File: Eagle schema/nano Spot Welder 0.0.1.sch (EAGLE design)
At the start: 32 parts, among them Q2 BC548, T1 BTA 41 / 600V, U1 NANO, U2 DISPLAY-NOKIA-5110, U3 DS18B20, X3 ~230V, X4 Mikro trafó

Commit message: - átszervezés
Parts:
- added Q1: BC548, transistor-npn:BC548
- added Q3: BC138, transistor-npn:BC548
- added R10, R9: 10k, resistor:R-EU_0204/7
- added VT1: Ventilátor, con-ptr500:AK300/2
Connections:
- net N$10 renamed A2
- net N$12 renamed A0
- net N$13 renamed D10
- net N$14 renamed +3.3V
- net N$2 renamed D9
- net N$27 renamed A1
- net N$3 renamed D8
- net N$30 renamed D11
- net N$4 renamed D7
- net N$5 renamed D6
- net N$6 renamed D5
- net N$7 renamed D4
- net N$8 renamed D3
- net N$9 renamed D2
- removed net N$11: R3.1, U1.D13
- removed net N$17: BUZZER1.2, Q2.C
- new net A3: R10.1, U1.A3
- new net D12: R9.2, U1.D12, U1.D13
- new net D13: R3.1
- new net N$3: BUZZER1.1, Q2.C
- new net N$4: Q1.B, R9.1
- new net N$5: Q3.B, R10.2
- new net N$6: Q3.C, VT1-1.KL
- net GND: now also Q3.E; no longer U1.GND2
- net MOC: now also Q1.E; no longer U1.D12
- net N$28: now also R5.1
- net N$33: no longer R5.1
- net VCC: now also BUZZER1.2, Q1.C, VT1-2.KL; no longer BUZZER1.1
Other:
- moved on the sheet: B1, BUZZER1, C10, C9, F1, KY-040, LED1, LED2, OK1, OK2, Q2, R1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

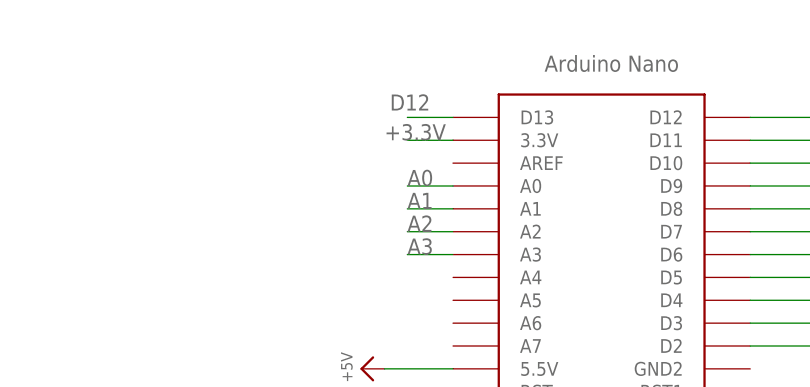
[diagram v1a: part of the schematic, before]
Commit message: - kijelzés finomítás - DS18B20 kiiktatása a próbák alatt
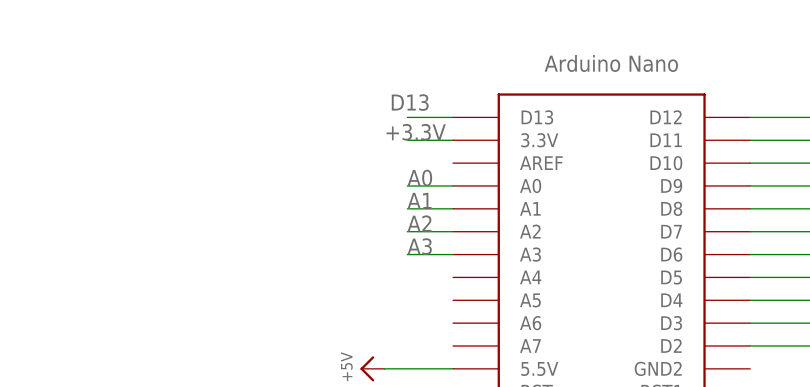
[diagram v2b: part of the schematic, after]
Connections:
- net D12: no longer U1.D13
- net D13: now also U1.D13
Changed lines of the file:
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@@
 <label x="-17.78" y="33.02" size="1.778" layer="95"/>
+</segment>
+<segment>
+<pinref part="U1" gate="G$1" pin="D13"/>
+<wire x1="-48.26" y1="119.38" x2="-53.34" y2="119.38" width="0.1524" layer="91"/>
+<label x="-50.8" y="121.92" size="1.778" layer="95" rot="R180"/>
 </segment>
 </net>
@@
 <label x="-101.6" y="-22.86" size="1.778" layer="95"/>
 </segment>
-<segment>
-<pinref part="U1" gate="G$1" pin="D13"/>
-<wire x1="-48.26" y1="119.38" x2="-53.34" y2="119.38" width="0.1524" layer="91"/>
-<label x="-50.8" y="121.92" size="1.778" layer="95" rot="R180"/>
-</segment>
 </net>

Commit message: - Eagle schema update
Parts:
- added D1: 1N4148, diode:1N4148DO35-10
- added J1: (no value), SparkFun-Connectors:CONN_03X22X3_SILK_MALE_PTH
- added R11: 1k, resistor:R-EU_0204/7
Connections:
- new net RST: J1.5, R11.1, U1.RST
- net D11: now also J1.4
- net D12: now also J1.1
- net D13: now also J1.3
- net GND: now also D1.A, J1.6, U1.GND2
- net N$6: now also D1.C
- net VCC: now also J1.2, R11.2, U1.AREF
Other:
- note added: "ISP"
- note added: "KY-040 Rotary Encoder"
- note added: "MOT Temperature Measurement"
- moved on the sheet: LED2, R1, R7, R8, S1, U2

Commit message: - próbapanel javítgatások
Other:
- note added: "CLK"
- note added: "DT"
- note added: "SW"
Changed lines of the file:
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@@
 <text x="116.84" y="45.72" size="1.778" layer="91">KY-040 Rotary Encoder</text>
 <text x="109.22" y="-20.32" size="1.778" layer="91">MOT Temperature Measurement</text>
+<text x="88.9" y="63.5" size="1.778" layer="91">CLK</text>
+<text x="88.9" y="68.58" size="1.778" layer="91">SW</text>
+<text x="88.9" y="66.04" size="1.778" layer="91">DT</text>
 </plain>
 <instances>

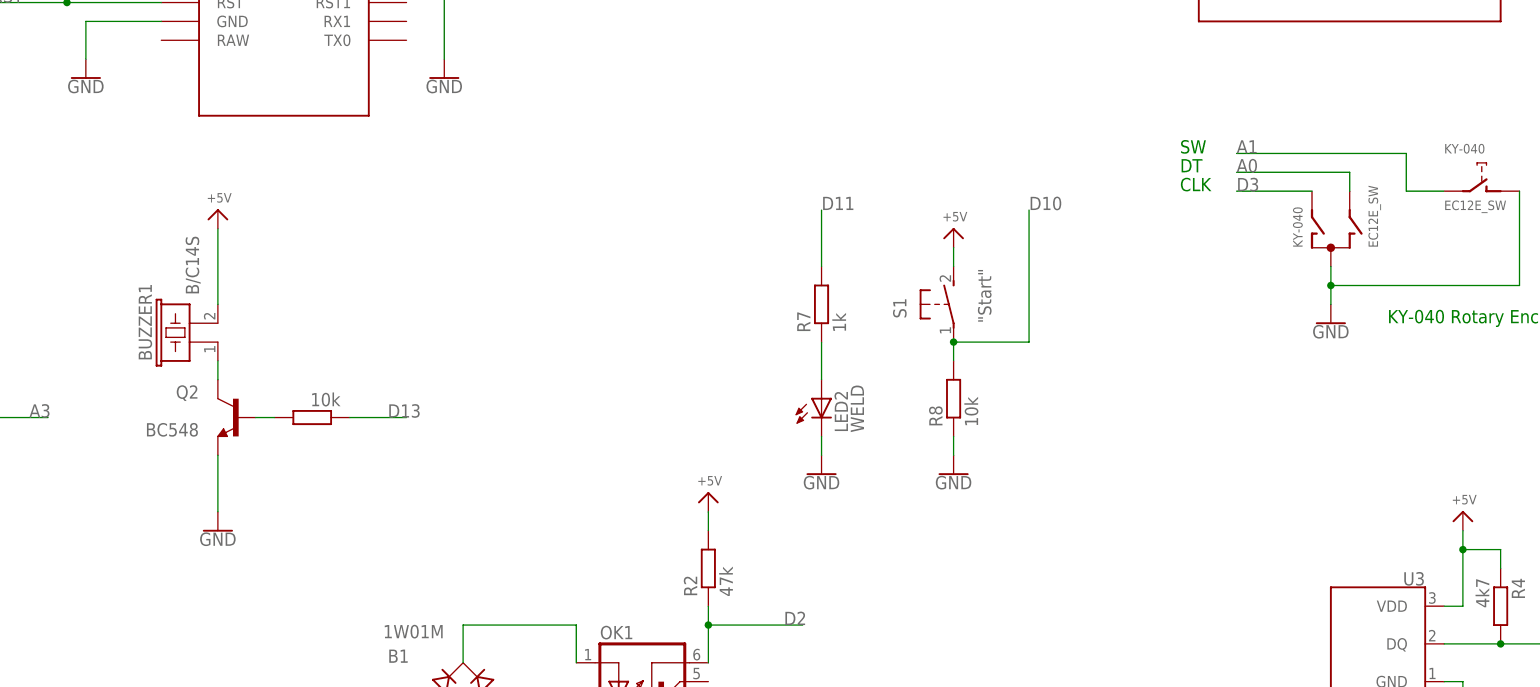
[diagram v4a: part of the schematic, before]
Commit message: -Rotary Encoder 1uF
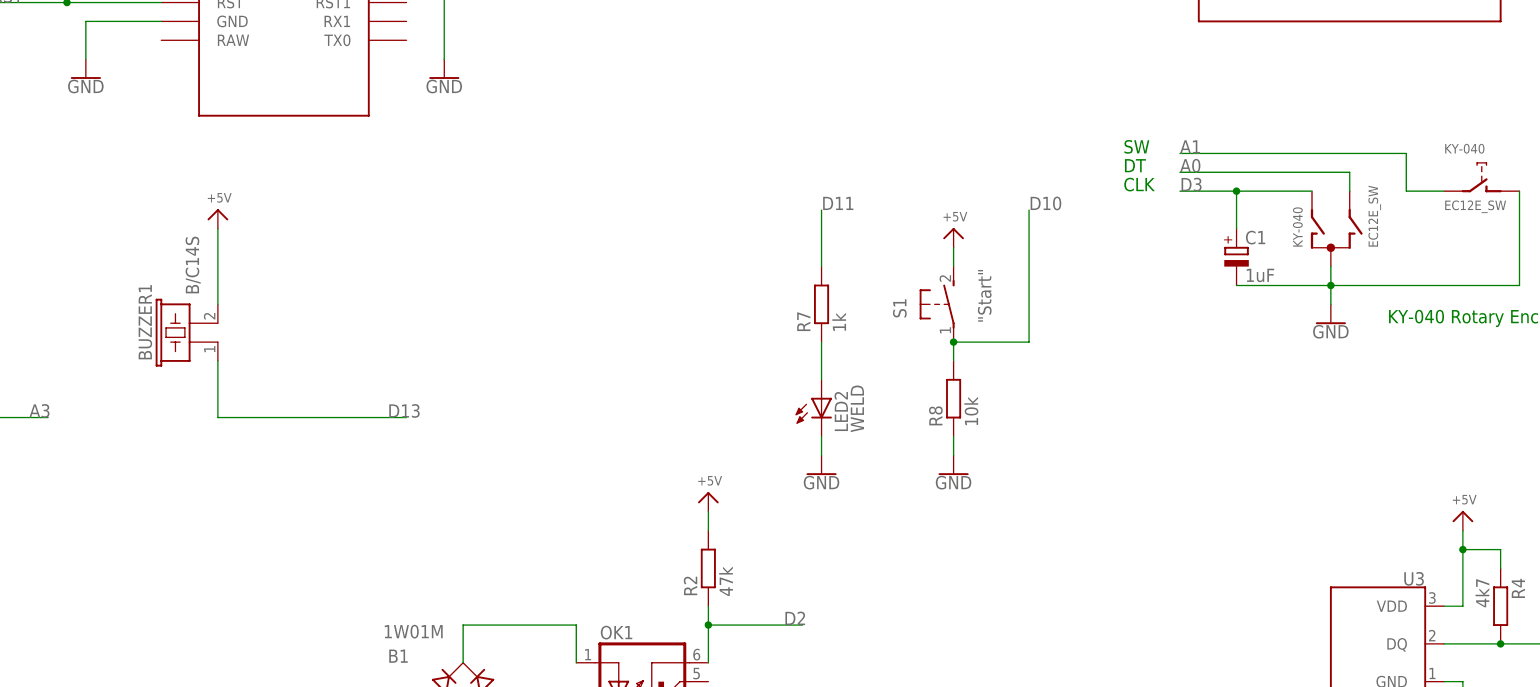
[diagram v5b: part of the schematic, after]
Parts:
- removed Q2: BC548, transistor-npn:BC548
- removed R3: 10k, resistor:R-EU_0204/7
- added C1: 1uF, rcl:CPOL-EUE5-5
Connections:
- removed net N$15: Q2.B, R3.2
- removed net N$3: BUZZER1.1, Q2.C
- net D13: now also BUZZER1.1; no longer R3.1
- net D3: now also C1.+
- net GND: now also C1.-; no longer Q2.E
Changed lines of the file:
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@@
 <part name="R1" library="resistor" library_urn="urn:adsk.eagle:library:348" deviceset="R-EU_" device="0204/7" package3d_urn="urn:adsk.eagle:package:25945/1" value="390R"/>
 <part name="OK1" library="optocoupler" library_urn="urn:adsk.eagle:library:320" deviceset="4N35" device="" package3d_urn="urn:adsk.eagle:package:21942/1" value="4N25"/>
-<part name="Q2" library="transistor-npn" library_urn="urn:adsk.eagle:library:398" deviceset="BC548*" device="" package3d_urn="urn:adsk.eagle:package:28989/2"/>
 <part name="B1" library="rectifier" library_urn="urn:adsk.eagle:library:336" deviceset="RB1A" device="" package3d_urn="urn:adsk.eagle:package:23866/1" value="1W01M"/>
 <part name="LED1" library="led" library_urn="urn:adsk.eagle:library:259" deviceset="LED" device="" package3d_urn="urn:adsk.eagle:package:15825/1" value="TRIAC CONTR"/>
@@
 <part name="GND4" library="SparkFun-PowerSymbols" library_urn="urn:adsk.eagle:library:530" deviceset="GND" device=""/>
 <part name="GND6" library="SparkFun-PowerSymbols" library_urn="urn:adsk.eagle:library:530" deviceset="GND" device=""/>
-<part name="R3" library="resistor" library_urn="urn:adsk.eagle:library:348" deviceset="R-EU_" device="0204/7" package3d_urn="urn:adsk.eagle:package:25945/1" value="10k"/>
 <part name="BUZZER1" library="buzzer" library_urn="urn:adsk.eagle:library:113" deviceset="B/C14S" device="" package3d_urn="urn:adsk.eagle:package:5279/1"/>
-<part name="GND8" library="SparkFun-PowerSymbols" library_urn="urn:adsk.eagle:library:530" deviceset="GND" device=""/>
 <part name="P+4" library="audio amplifier example" library_urn="urn:adsk.eagle:library:970892" deviceset="VCC" device="" value="+5V"/>
 <part name="GND9" library="SparkFun-PowerSymbols" library_urn="urn:adsk.eagle:library:530" deviceset="GND" device=""/>
@@
 <part name="P+9" library="audio amplifier example" library_urn="urn:adsk.eagle:library:970892" deviceset="VCC" device="" value="+5V"/>
 <part name="GND13" library="SparkFun-PowerSymbols" library_urn="urn:adsk.eagle:library:530" deviceset="GND" device=""/>
+<part name="C1" library="rcl" library_urn="urn:adsk.eagle:library:334" deviceset="CPOL-EU" device="E5-5" package3d_urn="urn:adsk.eagle:package:23367/1" value="1uF"/>
 </parts>
 <sheets>
@@
 <text x="116.84" y="45.72" size="1.778" layer="91">KY-040 Rotary Encoder</text>
 <text x="109.22" y="-20.32" size="1.778" layer="91">MOT Temperature Measurement</text>
-<text x="88.9" y="63.5" size="1.778" layer="91">CLK</text>
-<text x="88.9" y="68.58" size="1.778" layer="91">SW</text>
-<text x="88.9" y="66.04" size="1.778" layer="91">DT</text>
+<text x="81.28" y="63.5" size="1.778" layer="91">CLK</text>
+<text x="81.28" y="68.58" size="1.778" layer="91">SW</text>
+<text x="81.28" y="66.04" size="1.778" layer="91">DT</text>
 </plain>
 <instances>
@@
 <instance part="OK1" gate="G$1" x="17.78" y="-2.54">
 <attribute name="MPN" x="17.78" y="-20.32" size="1.778" layer="96" display="off"/>
-</instance>
-<instance part="Q2" gate="G$1" x="-38.1" y="33.02" smashed="yes" rot="MR0">
-<attribute name="NAME" x="-43.18" y="35.56" size="1.778" layer="95" rot="MR0"/>
-<attribute name="VALUE" x="-43.18" y="30.48" size="1.778" layer="96" rot="MR0"/>
 </instance>
 <instance part="B1" gate="1" x="-7.62" y="-5.08" smashed="yes" rot="R90">
@@
 <instance part="GND4" gate="1" x="127" y="-12.7"/>
 <instance part="GND6" gate="1" x="81.28" y="93.98"/>
-<instance part="R3" gate="G$1" x="-27.94" y="33.02" smashed="yes" rot="R180">
-<attribute name="VALUE" x="-24.13" y="36.322" size="1.778" layer="96" rot="R180"/>
-</instance>
 <instance part="BUZZER1" gate="G$1" x="-43.18" y="43.18" rot="R90"/>
-<instance part="GND8" gate="1" x="-40.64" y="17.78"/>
 <instance part="P+4" gate="VCC" x="127" y="20.32"/>
 <instance part="GND9" gate="1" x="-7.62" y="-15.24"/>
@@
 <instance part="P+9" gate="VCC" x="-60.96" y="127"/>
 <instance part="GND13" gate="1" x="-10.16" y="78.74"/>
+<instance part="C1" gate="G$1" x="96.52" y="55.88"/>
 </instances>
 <busses>
@@
 <wire x1="134.62" y1="50.8" x2="109.22" y2="50.8" width="0.1524" layer="91"/>
 <junction x="109.22" y="50.8"/>
+<wire x1="109.22" y1="50.8" x2="96.52" y2="50.8" width="0.1524" layer="91"/>
+<pinref part="C1" gate="G$1" pin="-"/>
 </segment>
 <segment>
@@
 <pinref part="GND2" gate="1" pin="GND"/>
 <wire x1="25.4" y1="-7.62" x2="25.4" y2="-12.7" width="0.1524" layer="91"/>
-</segment>
-<segment>
-<pinref part="GND8" gate="1" pin="GND"/>
-<pinref part="Q2" gate="G$1" pin="E"/>
-<wire x1="-40.64" y1="20.32" x2="-40.64" y2="27.94" width="0.1524" layer="91"/>
 </segment>
 <segment>
@@
 </segment>
 </net>
-<net name="N$15" class="0">
-<segment>
-<pinref part="R3" gate="G$1" pin="2"/>
-<pinref part="Q2" gate="G$1" pin="B"/>
-<wire x1="-33.02" y1="33.02" x2="-35.56" y2="33.02" width="0.1524" layer="91"/>
-</segment>
-</net>
 <net name="A2" class="0">
 <segment>
@@
 <pinref part="KY-040" gate="G$1" pin="A"/>
 <wire x1="106.68" y1="63.5" x2="96.52" y2="63.5" width="0.1524" layer="91"/>
-<label x="96.52" y="63.5" size="1.778" layer="95"/>
+<label x="88.9" y="63.5" size="1.778" layer="95"/>
+<wire x1="96.52" y1="63.5" x2="88.9" y2="63.5" width="0.1524" layer="91"/>
+<wire x1="96.52" y1="58.42" x2="96.52" y2="63.5" width="0.1524" layer="91"/>
+<junction x="96.52" y="63.5"/>
+<pinref part="C1" gate="G$1" pin="+"/>
 </segment>
 </net>
@@
 <pinref part="KY-040" gate="G$1" pin="B"/>
 <wire x1="111.76" y1="63.5" x2="111.76" y2="66.04" width="0.1524" layer="91"/>
-<wire x1="111.76" y1="66.04" x2="96.52" y2="66.04" width="0.1524" layer="91"/>
-<label x="96.52" y="66.04" size="1.778" layer="95"/>
+<wire x1="111.76" y1="66.04" x2="88.9" y2="66.04" width="0.1524" layer="91"/>
+<label x="88.9" y="66.04" size="1.778" layer="95"/>
 </segment>
 <segment>
@@
 <wire x1="124.46" y1="63.5" x2="119.38" y2="63.5" width="0.1524" layer="91"/>
 <wire x1="119.38" y1="63.5" x2="119.38" y2="68.58" width="0.1524" layer="91"/>
-<wire x1="119.38" y1="68.58" x2="96.52" y2="68.58" width="0.1524" layer="91"/>
-<label x="96.52" y="68.58" size="1.778" layer="95"/>
+<wire x1="119.38" y1="68.58" x2="88.9" y2="68.58" width="0.1524" layer="91"/>
+<label x="88.9" y="68.58" size="1.778" layer="95"/>
 </segment>
 <segment>
@@
 <net name="D13" class="0">
 <segment>
-<pinref part="R3" gate="G$1" pin="1"/>
-<wire x1="-22.86" y1="33.02" x2="-15.24" y2="33.02" width="0.1524" layer="91"/>
 <label x="-17.78" y="33.02" size="1.778" layer="95"/>
+<pinref part="BUZZER1" gate="G$1" pin="1"/>
+<wire x1="-15.24" y1="33.02" x2="-40.64" y2="33.02" width="0.1524" layer="91"/>
+<wire x1="-40.64" y1="33.02" x2="-40.64" y2="40.64" width="0.1524" layer="91"/>
 </segment>
 <segment>
@@
 <junction x="25.4" y="5.08"/>
 <label x="35.56" y="5.08" size="1.778" layer="95"/>
-</segment>
-</net>
-<net name="N$3" class="0">
-<segment>
-<pinref part="Q2" gate="G$1" pin="C"/>
-<pinref part="BUZZER1" gate="G$1" pin="1"/>
-<wire x1="-40.64" y1="38.1" x2="-40.64" y2="40.64" width="0.1524" layer="91"/>
 </segment>
 </net>
@@
 packages will not be understood (or retained) with this version.
 </note>
+<note version="8.4" severity="warning">
+Since Version 8.4, EAGLE supports properties for SPICE simulation.
+Probes in schematics and SPICE mapping objects found in parts and library devices
+will not be understood with this version. Update EAGLE to the latest version
+for full support of SPICE simulation.
+</note>
 </compatibility>
